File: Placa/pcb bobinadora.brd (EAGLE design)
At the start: 107.6 x 80 mm, 20 parts, among them IC1 PIC16F84AP, Q1 4 MhZ, SW1 MOMENTARY, SW2 MOMENTARY, SW3 MOMENTARY, X1 87758-3416

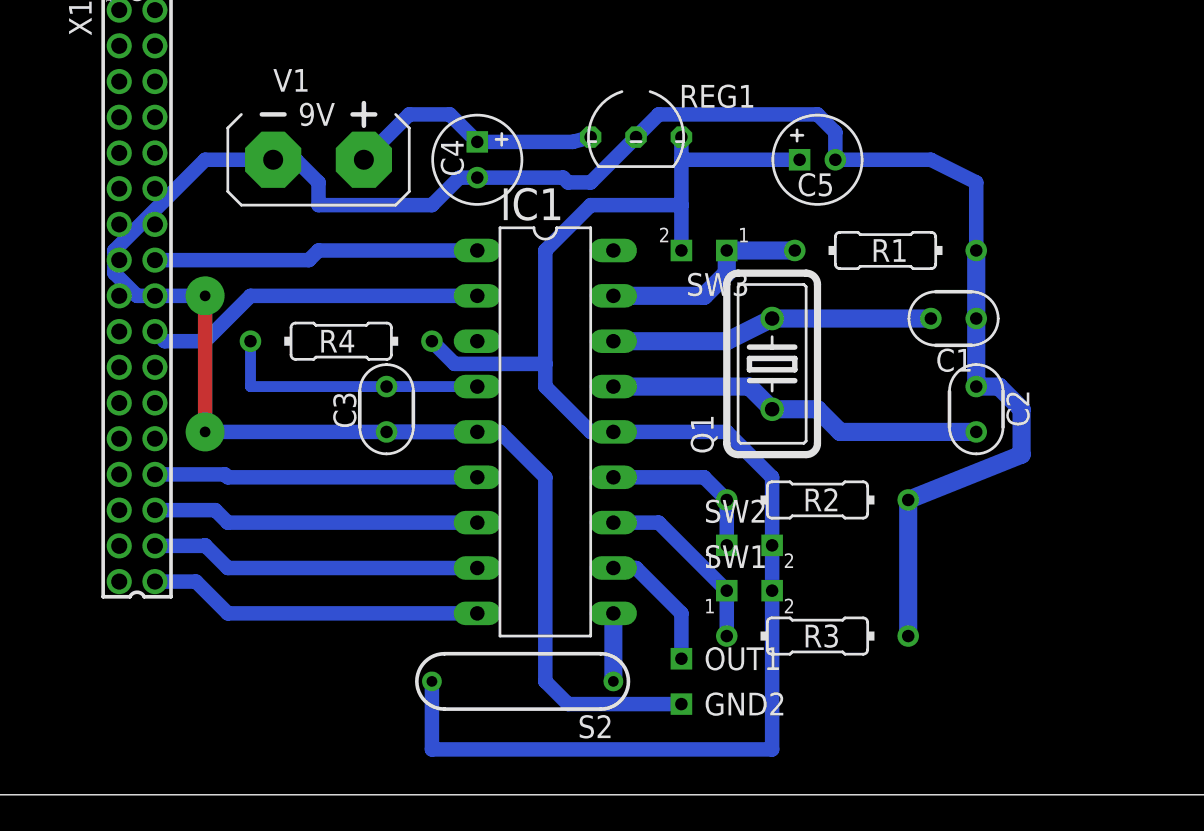
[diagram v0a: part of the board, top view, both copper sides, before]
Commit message: cambios para acomodar los botones
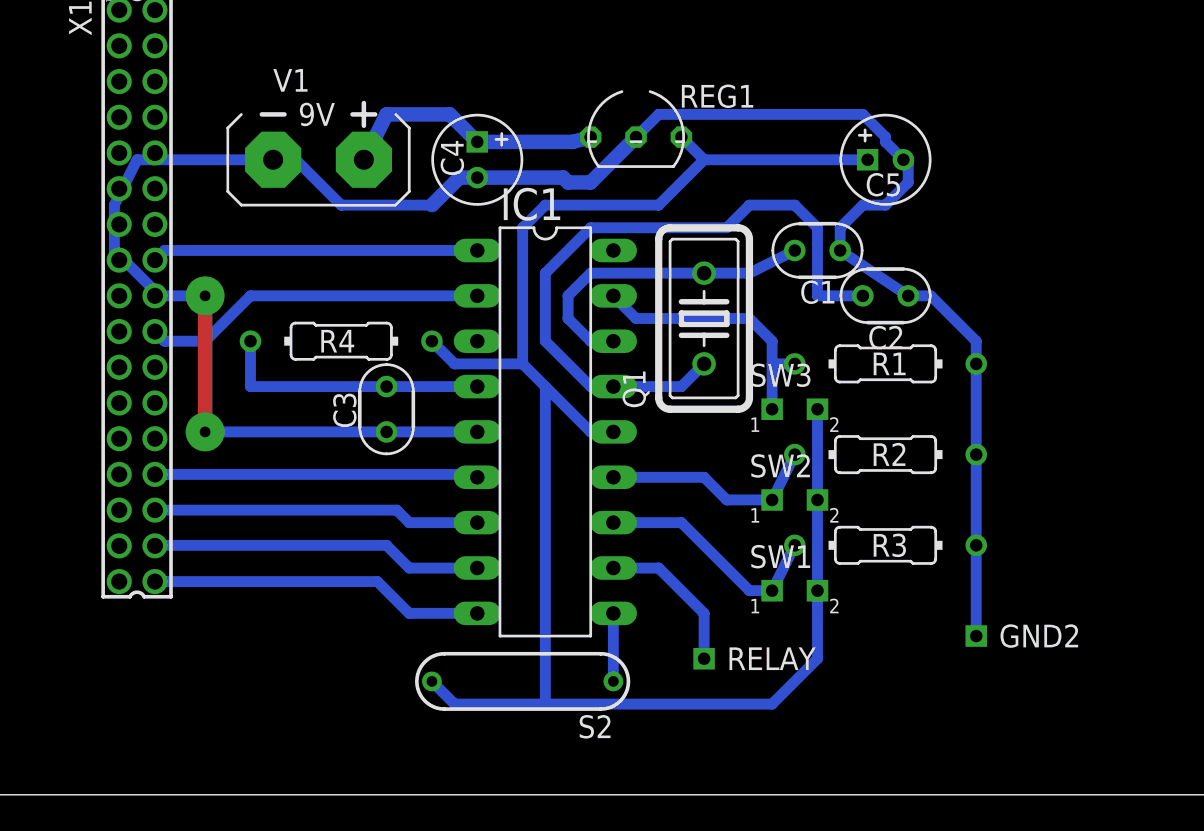
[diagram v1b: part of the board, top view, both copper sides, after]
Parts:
- removed OUT1: OUT(T), gm-supply:SQUARE
- added RELAY: OUT(T), gm-supply:SQUARE
- moved GND2 16.9 mm to (61.0, 8.89)
- moved SW3 10.2 mm to (50.8, 21.6), turned to 0 degrees
- moved C1 8.52 mm to (52.1, 30.5)
- moved C2 8.13 mm to (55.9, 27.9), turned to 180 degrees
- moved R1 6.35 mm to (55.9, 24.1)
- moved R3 6.35 mm to (55.9, 14.0)
- moved Q1 4.58 mm to (45.7, 26.7)
- moved R2 4.58 mm to (55.9, 19.1)
- moved C5 3.81 mm to (55.9, 35.6)
- moved SW2 3.59 mm to (50.8, 16.5)
- moved SW1 2.54 mm to (50.8, 11.4)
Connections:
- net OUT: now also RELAY.1; no longer OUT1.1
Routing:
- net GND: track 147.5 -> 115.6 mm
- net N$12: track 21.4 -> 38.0 mm
- net PWR: track 89.0 -> 97.5 mm
- net N$9: track 12.0 -> 15.0 mm
- net N$7: track 10.5 -> 13.3 mm
- net N$8: track 9.42 -> 12.3 mm
- net OUT: track 7.40 -> 8.67 mm
- net N$18: track 14.4 -> 14.9 mm

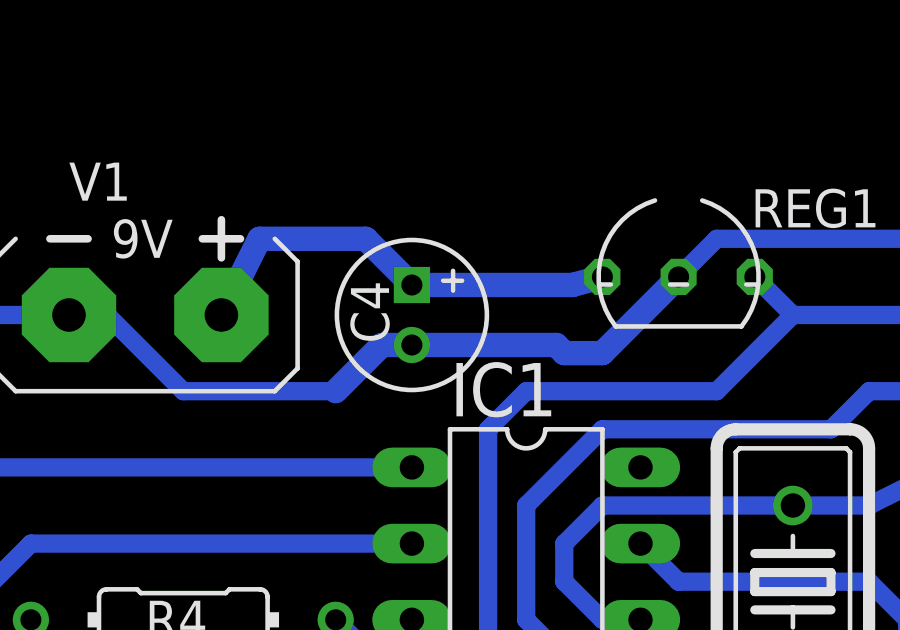
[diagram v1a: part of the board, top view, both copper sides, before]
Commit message: cambio x traza mas fina
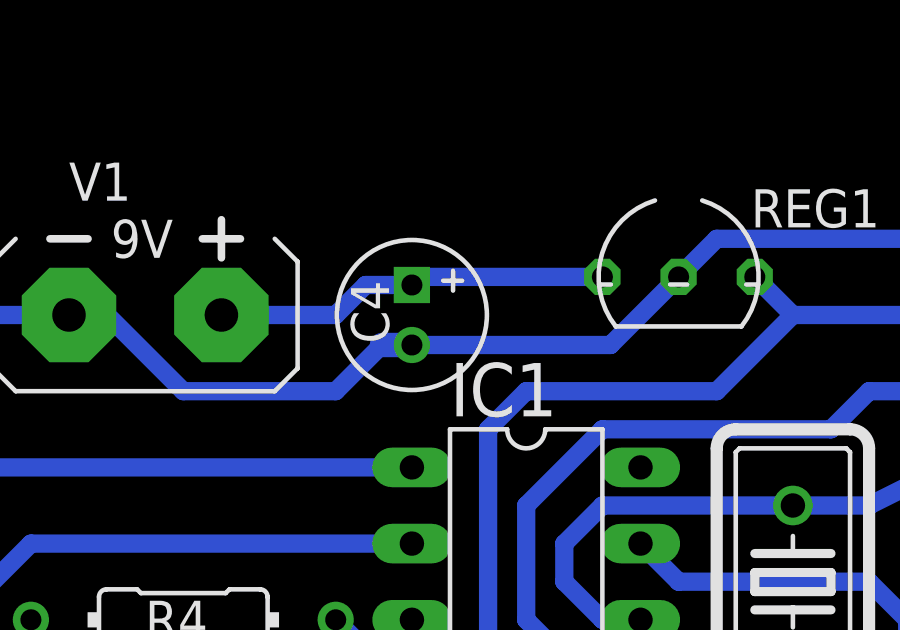
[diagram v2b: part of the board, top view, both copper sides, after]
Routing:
- net N$18: track 14.9 -> 13.2 mm
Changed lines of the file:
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@@
 <wire x1="17.78" y1="20.32" x2="17.78" y2="27.94" width="0.8128" layer="1"/>
 <wire x1="33.02" y1="34.56" x2="32.02" y2="34.56" width="0.8128" layer="16"/>
-<wire x1="32.02" y1="34.56" x2="30.48" y2="33.02" width="0.8128" layer="16"/>
-<wire x1="33.02" y1="34.56" x2="37.83" y2="34.56" width="0.8128" layer="16"/>
-<wire x1="37.83" y1="34.56" x2="38.1" y2="34.29" width="0.8128" layer="16"/>
-<wire x1="38.1" y1="34.29" x2="39.37" y2="34.29" width="0.8128" layer="16"/>
-<wire x1="39.37" y1="34.29" x2="41.91" y2="36.83" width="0.8128" layer="16"/>
 <contactref element="GND2" pad="1"/>
 <wire x1="60.96" y1="8.89" x2="60.96" y2="13.97" width="0.6096" layer="16"/>
@@
 <wire x1="12.7" y1="33.02" x2="13.97" y2="35.56" width="0.6096" layer="16"/>
 <wire x1="13.97" y1="35.56" x2="21.59" y2="35.56" width="0.6096" layer="16"/>
-<wire x1="17.78" y1="27.94" x2="17.78" y2="27.94" width="0" layer="19" extent="1-16"/>
 <wire x1="21.59" y1="35.56" x2="22.86" y2="35.56" width="0.6096" layer="16"/>
 <wire x1="22.86" y1="35.56" x2="25.4" y2="33.02" width="0.6096" layer="16"/>
 <wire x1="25.4" y1="33.02" x2="30.48" y2="33.02" width="0.6096" layer="16"/>
+<wire x1="17.78" y1="27.94" x2="17.78" y2="27.94" width="0" layer="19" extent="1-16"/>
+<wire x1="33.02" y1="34.56" x2="39.64" y2="34.56" width="0.6096" layer="16"/>
+<wire x1="39.64" y1="34.56" x2="41.91" y2="36.83" width="0.6096" layer="16"/>
+<wire x1="32.02" y1="34.56" x2="30.48" y2="33.02" width="0.6096" layer="16"/>
 </signal>
 <signal name="N$7">
@@
 <contactref element="C4" pad="+"/>
 <contactref element="REG1" pad="1"/>
-<wire x1="26.67" y1="35.56" x2="27.94" y2="38.1" width="0.8128" layer="16"/>
-<wire x1="27.94" y1="38.1" x2="31.48" y2="38.1" width="0.8128" layer="16"/>
-<wire x1="31.48" y1="38.1" x2="33.02" y2="36.56" width="0.8128" layer="16"/>
-<wire x1="33.02" y1="36.56" x2="38.37" y2="36.56" width="0.8128" layer="16"/>
-<wire x1="38.37" y1="36.56" x2="39.37" y2="36.83" width="0.8128" layer="16"/>
+<wire x1="39.37" y1="36.83" x2="33.29" y2="36.83" width="0.6096" layer="16"/>
+<wire x1="33.29" y1="36.83" x2="33.02" y2="36.56" width="0.6096" layer="16"/>
+<wire x1="33.02" y1="36.56" x2="31.48" y2="36.56" width="0.6096" layer="16"/>
+<wire x1="31.48" y1="36.56" x2="30.48" y2="35.56" width="0.6096" layer="16"/>
+<wire x1="30.48" y1="35.56" x2="26.67" y2="35.56" width="0.6096" layer="16"/>
 </signal>
 <signal name="PWR">

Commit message: final
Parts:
- removed V1: 9VBATTERY, gm-supply:AB9V
- removed X1: 87758-3416, con-molex:87758-3416
- added +9V1: +9V(T), gm-supply:SQUARE
- added JP2: (no value), pinhead:1X16
- moved C5 14.0 mm to (41.9, 36.8), turned to 270 degrees
- moved REG1 12.8 mm to (29.2, 38.1)
- moved C2 10.9 mm to (66.0, 31.8), turned to 270 degrees
- moved SW1 9.67 mm to (59.7, 7.62)
- moved C4 9.25 mm to (24.1, 38.1)
- moved C1 8.98 mm to (61.0, 31.8), turned to 270 degrees
- moved SW2 8.98 mm to (59.7, 15.2)
- moved SW3 8.98 mm to (59.7, 22.9)
- moved GND2 8.52 mm to (68.6, 5.08)
- moved R1 8.03 mm to (63.5, 26.7)
- moved R3 8.03 mm to (63.5, 11.4)
- moved R2 7.62 mm to (63.5, 19.1)
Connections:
- removed net N$18: C4.+, REG1.1, V1.+
- new net N$17: JP2.1, JP2.5
- net GND: no longer V1.-, X1.18
- net N$1: now also JP2.11; no longer X1.28
- net N$2: now also JP2.12; no longer X1.30
- net N$3: now also JP2.13; no longer X1.32
- net N$4: now also JP2.14; no longer X1.34
- net N$5: now also JP2.4; no longer X1.16
- net N$6: now also JP2.6; no longer X1.20
- net PWR: now also +9V1.1, C4.+, JP2.2, REG1.1
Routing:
- net PWR: track 97.5 -> 188.4 mm
- net N$17: track 0.00 -> 16.3 mm
- net N$12: track 38.0 -> 53.7 mm
- net N$18: track 13.2 -> 0.00 mm
- net N$9: track 15.0 -> 27.5 mm
- net N$10: track 17.9 -> 29.3 mm
- net N$7: track 13.3 -> 24.7 mm
- net N$8: track 12.3 -> 22.6 mm
- net N$5: track 18.3 -> 22.9 mm
- net GND: track 115.4 -> 112.2 mm, vias 1 -> 2
- net N$1: track 18.1 -> 20.3 mm
- net N$6: track 19.3 -> 21.4 mm
- net N$2: track 18.3 -> 20.3 mm
- net N$3: track 18.6 -> 20.3 mm
- net N$4: track 18.8 -> 20.3 mm
